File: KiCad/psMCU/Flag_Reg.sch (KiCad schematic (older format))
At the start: 30 parts

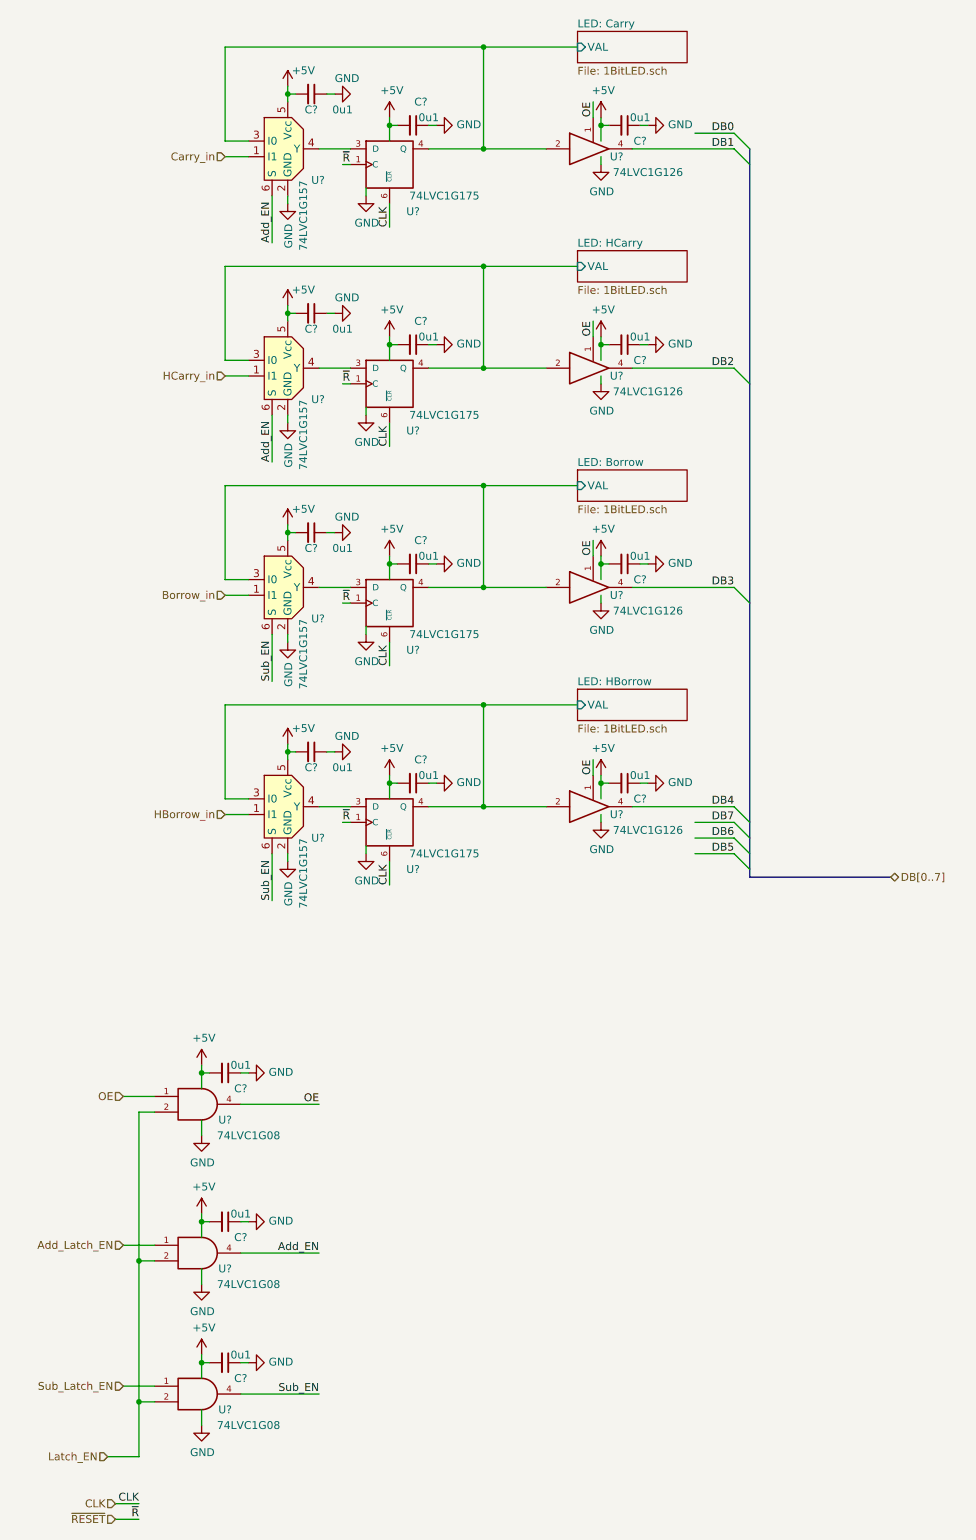
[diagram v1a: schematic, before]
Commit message: First ERC pass
    All unconnects solved, need to inspect Tristate errors.
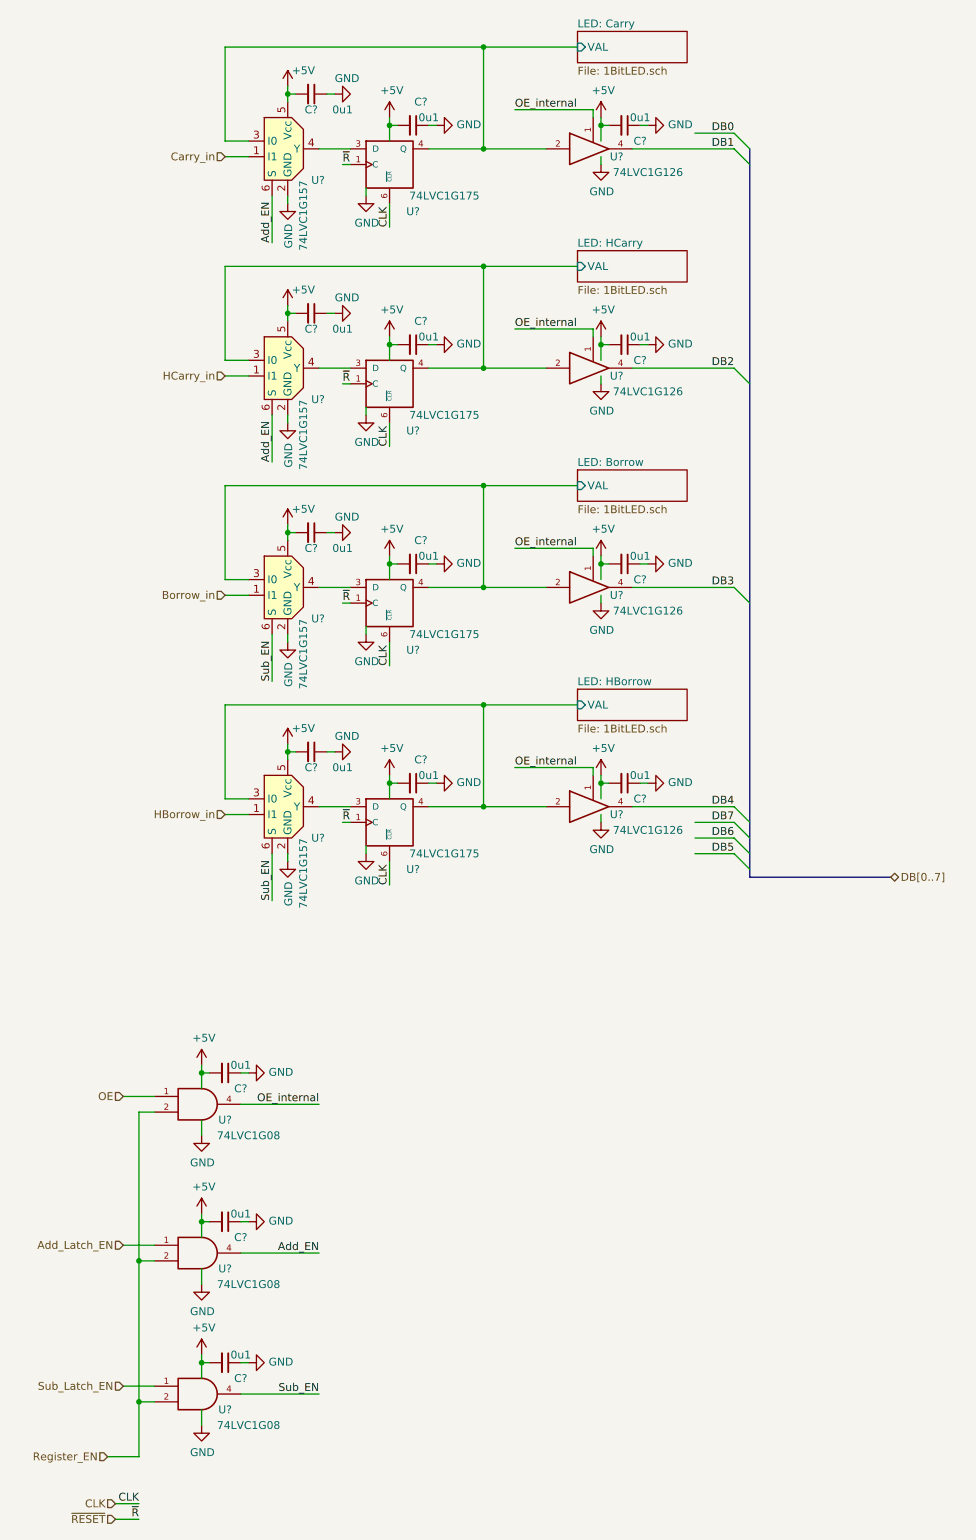
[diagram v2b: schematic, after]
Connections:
- net OE: no longer U?.1, U?.1, U?.1, U?.1, U?.4
- net Latch_EN renamed Register_EN
- new net OE_internal: U?.1, U?.1, U?.1, U?.1, U?.4
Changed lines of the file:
@@
 $Descr A4 8268 11693 portrait
 encoding utf-8
-Sheet 147 209
+Sheet 202 207
 Title "psMCU"
 Date ""
@@
 $EndDescr
 Text HLabel 1300 10400 0    50   Input ~ 0
-Latch_EN
+Register_EN
 Text HLabel 1400 9050 0    50   Input ~ 0
 Add_Latch_EN
@@
 	1400 8100 1600 8100
 Text Label 2650 8150 2    50   ~ 0
-OE
-Text Label 4400 5950 3    50   ~ 0
-OE
-Wire Wire Line
-	4400 5950 4400 6050
-Text Label 4400 4550 3    50   ~ 0
-OE
-Wire Wire Line
-	4400 4550 4400 4650
-Text Label 4400 3150 3    50   ~ 0
-OE
-Wire Wire Line
-	4400 3150 4400 3250
-Text Label 4400 1750 3    50   ~ 0
-OE
-Wire Wire Line
-	4400 1750 4400 1850
+OE_internal
 Wire Wire Line
 	2200 8900 2150 8900
@@
 Wire Wire Line
 	3700 1400 4300 1400
+Connection ~ 3700 1400
+Text Label 3900 6000 0    50   ~ 0
+OE_internal
+Wire Wire Line
+	4400 6000 3900 6000
+Wire Wire Line
+	4400 6000 4400 6050
+Text Label 3900 1800 0    50   ~ 0
+OE_internal
+Wire Wire Line
+	4400 1800 3900 1800
+Wire Wire Line
+	4400 1800 4400 1850
+Text Label 3900 3200 0    50   ~ 0
+OE_internal
+Wire Wire Line
+	4400 3200 3900 3200
+Wire Wire Line
+	4400 3200 4400 3250
+Text Label 3900 4600 0    50   ~ 0
+OE_internal
+Wire Wire Line
+	4400 4600 3900 4600
+Wire Wire Line
+	4400 4600 4400 4650
 Wire Bus Line
 	5400 2050 5400 6700
-Connection ~ 3700 1400
 $EndSCHEMATC

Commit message: Added some footprints, small optimisations
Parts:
- U? (x7): footprint (none) -> Package_TO_SOT_SMD:SOT-353_SC-70-5
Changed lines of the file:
@@
 F 0 "U?" H 4550 2000 50  0000 C CNN
 F 1 "74LVC1G126" H 4750 1900 50  0000 C CNN
-F 2 "" H 4400 2050 50  0001 C CNN
+F 2 "Package_TO_SOT_SMD:SOT-353_SC-70-5" H 4400 2050 50  0001 C CNN
 F 3 "http://www.ti.com/lit/sg/scyt129e/scyt129e.pdf" H 4400 2050 50  0001 C CNN
 	1    4400 2050
@@
 F 0 "U?" H 4550 3400 50  0000 C CNN
 F 1 "74LVC1G126" H 4750 3300 50  0000 C CNN
-F 2 "" H 4400 3450 50  0001 C CNN
+F 2 "Package_TO_SOT_SMD:SOT-353_SC-70-5" H 4400 3450 50  0001 C CNN
 F 3 "http://www.ti.com/lit/sg/scyt129e/scyt129e.pdf" H 4400 3450 50  0001 C CNN
 	1    4400 3450
@@
 F 0 "U?" H 4550 4800 50  0000 C CNN
 F 1 "74LVC1G126" H 4750 4700 50  0000 C CNN
-F 2 "" H 4400 4850 50  0001 C CNN
+F 2 "Package_TO_SOT_SMD:SOT-353_SC-70-5" H 4400 4850 50  0001 C CNN
 F 3 "http://www.ti.com/lit/sg/scyt129e/scyt129e.pdf" H 4400 4850 50  0001 C CNN
 	1    4400 4850
@@
 F 0 "U?" H 2050 9000 50  0000 C CNN
 F 1 "74LVC1G08" H 2200 8900 50  0000 C CNN
-F 2 "" H 1900 9100 50  0001 C CNN
+F 2 "Package_TO_SOT_SMD:SOT-353_SC-70-5" H 1900 9100 50  0001 C CNN
 F 3 "http://www.ti.com/lit/sg/scyt129e/scyt129e.pdf" H 1900 9100 50  0001 C CNN
 	1    1900 9100
@@
 F 0 "U?" H 2050 9900 50  0000 C CNN
 F 1 "74LVC1G08" H 2200 9800 50  0000 C CNN
-F 2 "" H 1900 10000 50  0001 C CNN
+F 2 "Package_TO_SOT_SMD:SOT-353_SC-70-5" H 1900 10000 50  0001 C CNN
 F 3 "http://www.ti.com/lit/sg/scyt129e/scyt129e.pdf" H 1900 10000 50  0001 C CNN
 	1    1900 10000
@@
 F 0 "U?" H 4550 6200 50  0000 C CNN
 F 1 "74LVC1G126" H 4750 6100 50  0000 C CNN
-F 2 "" H 4400 6250 50  0001 C CNN
+F 2 "Package_TO_SOT_SMD:SOT-353_SC-70-5" H 4400 6250 50  0001 C CNN
 F 3 "http://www.ti.com/lit/sg/scyt129e/scyt129e.pdf" H 4400 6250 50  0001 C CNN
 	1    4400 6250
@@
 F 0 "U?" H 2050 8050 50  0000 C CNN
 F 1 "74LVC1G08" H 2200 7950 50  0000 C CNN
-F 2 "" H 1900 8150 50  0001 C CNN
+F 2 "Package_TO_SOT_SMD:SOT-353_SC-70-5" H 1900 8150 50  0001 C CNN
 F 3 "http://www.ti.com/lit/sg/scyt129e/scyt129e.pdf" H 1900 8150 50  0001 C CNN
 	1    1900 8150

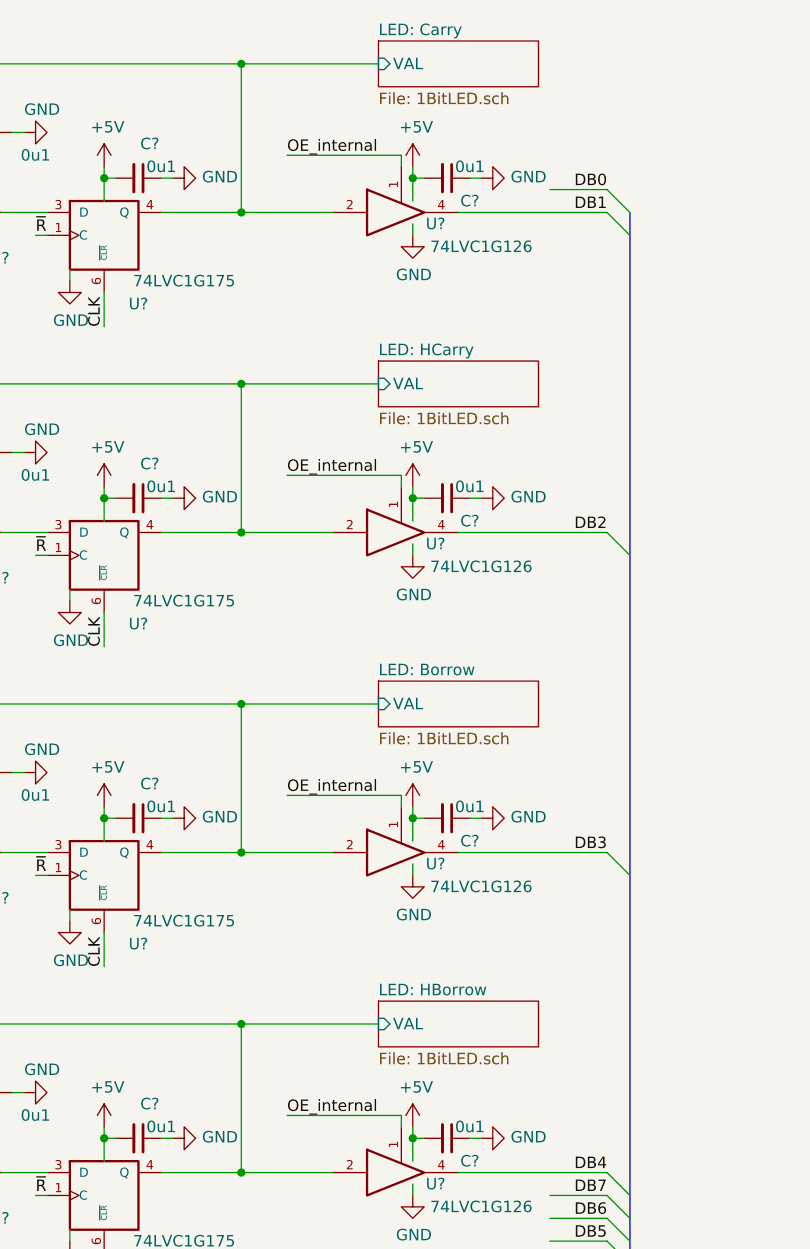
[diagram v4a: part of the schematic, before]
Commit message: Removed Single LED sheets
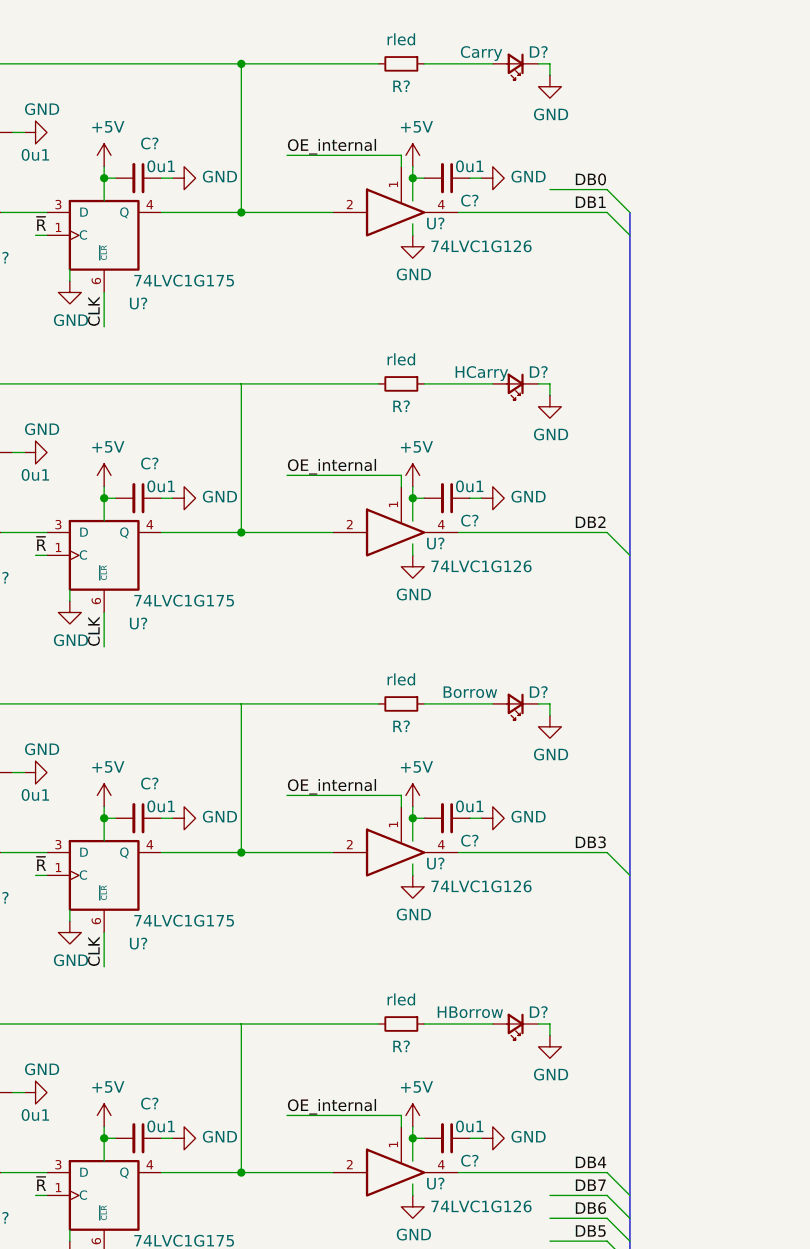
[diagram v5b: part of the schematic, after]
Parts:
- added D?: Carry, Diode_SMD:D_0603_1608Metric, symbol Device:LED_Small
- added D?: HCarry, Diode_SMD:D_0603_1608Metric, symbol Device:LED_Small
- added D?: Borrow, Diode_SMD:D_0603_1608Metric, symbol Device:LED_Small
- added D?: HBorrow, Diode_SMD:D_0603_1608Metric, symbol Device:LED_Small
- added R? (x4): rled, Resistor_SMD:R_0603_1608Metric, symbol Device:R_Small
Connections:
- net GND: now also D?.1 (K), D?.1 (K), D?.1 (K), D?.1 (K)
- net LED: Borrow/VAL: no longer names the net of U?.2, U?.3 (I0), U?.4 (Q)
- net LED: Borrow/VAL: now also R?.2
- net LED: Carry/VAL: no longer names the net of U?.2, U?.3 (I0), U?.4 (Q)
- net LED: Carry/VAL: now also R?.2
- net LED: HBorrow/VAL: no longer names the net of U?.2, U?.3 (I0), U?.4 (Q)
- net LED: HBorrow/VAL: now also R?.2
- net LED: HCarry/VAL: no longer names the net of U?.2, U?.3 (I0), U?.4 (Q)
- net LED: HCarry/VAL: now also R?.2
- new net: D?.2 (A), R?.1 (x4)

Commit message: First Schematic Draft done.
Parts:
- C415, C416, C417, C418, C419, C420, C421, C422, C423, C424, C425, C426, C427, C428, C429: renamed from C?; footprint Capacitor_SMD:C_0603_1608Metric -> NoRef_Footprints:C_0603_1608Metric_NoRef
- D415, D416, D417, D418: renamed from D?; footprint Diode_SMD:D_0603_1608Metric -> NoRef_Footprints:D_0603_1608Metric_NoRef
- R447, R448, R449, R450: renamed from R?; footprint Resistor_SMD:R_0603_1608Metric -> NoRef_Footprints:R_0603_1608Metric
- gave numbers to parts that had none: 15
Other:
- note added: "Borrow"
- note added: "Carry"
- note added: "Half-Borrow"
- note added: "Half-Carry"

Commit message: Small improvements.
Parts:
- renumbered C415 to C410, C416 to C411, C417 to C412, C418 to C413, C419 to C414, C420 to C415, C421 to C416, C422 to C417, C423 to C418, C424 to C419, C425 to C420, C426 to C421, C427 to C422, C428 to C423, C429 to C424, U399 to U394, U400 to U395, U401 to U396, U402 to U397, U403 to U398, U404 to U399, U405 to U400, U406 to U401, U407 to U402, U408 to U403, U409 to U404, U410 to U405, U411 to U406, U412 to U407, U413 to U408
